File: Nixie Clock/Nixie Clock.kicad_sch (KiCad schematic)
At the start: 101 parts, among them J1 Micro_SD_Card_Det1, Q1 SS8050, Q10 MPSA42/PMBTA42, Q11 MPSA92/PMBTA92, Q12 MPSA42/PMBTA42, Q13 MPSA92/PMBTA92, Q14 MPSA42/PMBTA42, Q15 MPSA92/PMBTA92, Q16 MPSA42/PMBTA42, Q17 MPSA42/PMBTA42, Q18 MPSA42/PMBTA42, Q19 MPSA42/PMBTA42, Q2 SS8050, Q4 MPSA92/PMBTA92, Q5 MPSA42/PMBTA42, Q6 MPSA42/PMBTA42, Q7 MPSA92/PMBTA92, Q8 MPSA42/PMBTA42, Q9 MPSA92/PMBTA92, SW3 SW_MEC_5G, SW4 SW_MEC_5G, U1 ESP32-WROOM-32E, U13 K155NA1, U4 CP2102N-Axx-xQFN28, U6 MCP23017_ML

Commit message: PCB routed
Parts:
- removed N1, N2, N3, N4: IN-6, nixies-us_IN-6, symbol nixies-us:IN-6
- removed NX1, NX2, NX3, NX4, NX5, NX6: IN-12A, nixies-us_IN-12, symbol nixies-us:IN-12A
- removed Q10, Q12, Q14, Q16, Q17, Q18, Q19, Q5, Q6, Q8: MPSA42/PMBTA42, symbol Simulation_SPICE:NPN
- removed Q11, Q13, Q15, Q4, Q7, Q9: MPSA92/PMBTA92, symbol Simulation_SPICE:PNP
- removed R20, R23, R24, R27, R28, R31, R32, R35, R36, R39, R40, R43, R48, R49, R50, R51: 4K7, symbol Device:R
- removed R21, R26, R30, R34, R38, R42: 10K, symbol Device:R
- removed R22, R25, R29, R33, R37, R41: 300K, symbol Device:R
- removed R44, R45, R46, R47: 15K, symbol Device:R
- removed SW3, SW4: SW_MEC_5G, symbol Switch:SW_MEC_5G
- added C11: 10uF, Capacitor_SMD:C_0603_1608Metric, symbol Device:C
- added H1, H2, H3, H4, H5, H6, H7, H8: MountingHole_Pad, MountingHole:MountingHole_3.2mm_M3_Pad_Via, symbol Mechanical:MountingHole_Pad
- added J1: Conn_02x13_Odd_Even, Connector_PinHeader_2.54mm:PinHeader_2x13_P2.54mm_Vertical, symbol Connector_Generic:Conn_02x13_Odd_Even
- added J3: Conn_02x13_Odd_Even, Connector_PinSocket_2.54mm:PinSocket_2x13_P2.54mm_Vertical, symbol Connector_Generic:Conn_02x13_Odd_Even
- added R13, R15, R16, R17: 10K, Resistor_SMD:R_0603_1608Metric, symbol Device:R
- added SW1, SW2: SW_Push, Button_Switch_SMD:SW_Push_SPST_NO_Alps_SKRK, symbol Switch:SW_Push
- C1: renamed from C14; footprint (none) -> Capacitor_SMD:C_0603_1608Metric
- C10: renamed from C2; footprint (none) -> Capacitor_SMD:C_0603_1608Metric
- C2: renamed from C20; footprint (none) -> Capacitor_SMD:C_0603_1608Metric
- C3: renamed from C8; footprint (none) -> Capacitor_SMD:C_0603_1608Metric
- C4: renamed from C9; footprint (none) -> Capacitor_SMD:C_0603_1608Metric
- C5: renamed from C11; footprint (none) -> Capacitor_SMD:C_0603_1608Metric
- C6: renamed from C10; footprint (none) -> Capacitor_SMD:C_0603_1608Metric
- C7: renamed from C12; footprint (none) -> Capacitor_SMD:C_0603_1608Metric
- C8: renamed from C13; footprint (none) -> Capacitor_SMD:C_0603_1608Metric
- C9: renamed from C1; footprint (none) -> Capacitor_SMD:C_0603_1608Metric
- D1: renamed from D11; footprint (none) -> Diode_SMD:D_MiniMELF
- D10: renamed from D19; footprint (none) -> Diode_SMD:D_MiniMELF
- D11: renamed from D20; footprint (none) -> Diode_SMD:D_MiniMELF
- D2: renamed from D12; footprint (none) -> Diode_SMD:D_MiniMELF
- D3: renamed from D13; footprint (none) -> Diode_SMD:D_MiniMELF
- D4: renamed from D14; footprint (none) -> Diode_SMD:D_MiniMELF
- D5: renamed from D15; footprint (none) -> Diode_SMD:D_MiniMELF
- D6: renamed from D21; value ZM4764A 100V -> 1N4764A 100V; footprint (none) -> Diode_THT:D_DO-41_SOD81_P7.62mm_Horizontal
- D7: renamed from D16; footprint (none) -> Diode_SMD:D_MiniMELF
- D8: renamed from D17; footprint (none) -> Diode_SMD:D_MiniMELF
- D9: renamed from D18; footprint (none) -> Diode_SMD:D_MiniMELF
- J2: renamed from J1; footprint (none) -> Connector_Card:microSD_HC_Hirose_DM3AT-SF-PEJM5
- R1: renamed from R16; footprint (none) -> Resistor_SMD:R_0603_1608Metric
- R10: renamed from R14; footprint (none) -> Resistor_SMD:R_0603_1608Metric
- R11: renamed from R15; footprint (none) -> Resistor_SMD:R_0603_1608Metric
- R12: renamed from R1; value 1K -> 10K; footprint (none) -> Resistor_SMD:R_0603_1608Metric
- R14: renamed from R2; footprint (none) -> Resistor_SMD:R_0603_1608Metric
- R2: renamed from R56; footprint (none) -> Resistor_SMD:R_0603_1608Metric
- R3: renamed from R57; footprint (none) -> Resistor_SMD:R_0603_1608Metric
- R4: renamed from R10; footprint (none) -> Resistor_SMD:R_0603_1608Metric
- R5: renamed from R11; footprint (none) -> Resistor_SMD:R_0603_1608Metric
- R6: renamed from R12; footprint (none) -> Resistor_SMD:R_0603_1608Metric
- R7: renamed from R13; footprint (none) -> Resistor_SMD:R_0603_1608Metric
- R8: renamed from R9; footprint (none) -> Resistor_SMD:R_0603_1608Metric
- R9: renamed from R8; footprint (none) -> Resistor_SMD:R_0603_1608Metric
- U1: renamed from U13; footprint (none) -> Package_DIP:DIP-16_W7.62mm
- renumbered U1 to U2, U4 to U3, U6 to U4
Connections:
- net +180V: now also J1.2 (Pin_2), J3.2 (Pin_2)
- net +3.3V: now also C11.1, J1.6 (Pin_6), J3.6 (Pin_6), R13.1, R15.1, R16.1, R17.1
- net +5V: now also J1.3 (Pin_3), J3.3 (Pin_3)
- net EN: now also SW2.2
- net GND: now also C11.2, H1.1, H2.1, H3.1, H4.1, H5.1, H6.1, H7.1, H8.1, J1.1 (Pin_1), J1.4 (Pin_4), J3.1 (Pin_1), J3.4 (Pin_4), SW1.1, SW2.1
- net IO0: now also SW1.2
- net LEDIN: now also J1.5 (Pin_5), J3.5 (Pin_5)
- net MISO: now also R16.2
- net MOSI: now also R15.2
- net N1: now also J1.19 (Pin_19), J3.19 (Pin_19)
- net N2: now also J1.8 (Pin_8), J3.8 (Pin_8)
- net N3: now also J1.14 (Pin_14), J3.14 (Pin_14)
- net N4: now also J1.16 (Pin_16), J3.16 (Pin_16)
- net NCA: now also J1.7 (Pin_7), J3.7 (Pin_7)
- net NCB: now also J1.9 (Pin_9), J3.9 (Pin_9)
- net NCC: now also J1.11 (Pin_11), J3.11 (Pin_11)
- net NCD: now also J1.13 (Pin_13), J3.13 (Pin_13)
- net NX1: now also J1.15 (Pin_15), J3.15 (Pin_15)
- net NX2: now also J1.17 (Pin_17), J3.17 (Pin_17)
- net NX3: now also J1.10 (Pin_10), J3.10 (Pin_10)
- net NX4: now also J1.12 (Pin_12), J3.12 (Pin_12)
- net NX5: now also J1.18 (Pin_18), J3.18 (Pin_18)
- net NX6: now also J1.20 (Pin_20), J3.20 (Pin_20)
- net ROT1A: now also J1.25 (Pin_25), J3.25 (Pin_25)
- net ROT1B: now also J1.23 (Pin_23), J3.23 (Pin_23)
- net ROT1SW: now also J1.21 (Pin_21), J3.21 (Pin_21)
- net ROT2A: now also J1.26 (Pin_26), J3.26 (Pin_26)
- net ROT2B: now also J1.24 (Pin_24), J3.24 (Pin_24)
- net ROT2SW: now also J1.22 (Pin_22), J3.22 (Pin_22)
- net Nixie Tube/0: now reaches D11.2 (A), U1.16 (0)
- net Nixie Tube/1: now reaches D1.2 (A), U1.15 (1)
- net Nixie Tube/2: now reaches D2.2 (A), U1.8 (2)
- net Nixie Tube/3: now reaches D3.2 (A), U1.9 (3)
- net Nixie Tube/4: now reaches D4.2 (A), U1.13 (4)
- net Nixie Tube/5: now reaches D5.2 (A), U1.14 (5)
- net Nixie Tube/6: now reaches D7.2 (A), U1.11 (6)
- net Nixie Tube/7: now reaches D8.2 (A), U1.10 (7)
- net Nixie Tube/8: now reaches D9.2 (A), U1.1 (8)
- net Nixie Tube/9: now reaches D10.2 (A), U1.2 (9)
- net DAT2: now reaches J2.1 (DAT2)
- net DAT2: now also R13.2
- net DAT1: now reaches J2.8 (DAT1)
- net DAT1: now also R17.2
- net CTS: no longer names the net of U3.23 (~{CTS})
- net DCD: no longer names the net of U3.1 (~{DCD})
- net DSR: no longer names the net of U3.27 (~{DSR})
- net RI: no longer names the net of U3.2 (~{RI}/CLK)
- no-connect marks 16 -> 20
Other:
- added sheet Nixie Bulb (nixiebulb.kicad_sch)
- added sheet Nixie Bulb1 (nixiebulb.kicad_sch)
- added sheet Nixie Bulb2 (nixiebulb.kicad_sch)
- added sheet Nixie Bulb3 (nixiebulb.kicad_sch)
- added sheet Nixie Tube (nixietube.kicad_sch)
- added sheet Nixie Tube1 (nixietube.kicad_sch)
- added sheet Nixie Tube2 (nixietube.kicad_sch)
- added sheet Nixie Tube3 (nixietube.kicad_sch)
- added sheet Nixie Tube4 (nixietube.kicad_sch)
- added sheet Nixie Tube5 (nixietube.kicad_sch)
- note added: "B2B Conn"
- note added: "KiCAD Stuff"
- title: (none) -> Nixie Clock
- moved on the sheet: C10, J2, R12, R14

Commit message: Add MAX3421 and CH334R for mass storage device capability
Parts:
- added C54, C55, C59: 100nF, Capacitor_SMD:C_0603_1608Metric, symbol Device:C
- added C56: 10uF, Capacitor_SMD:C_0603_1608Metric, symbol Device:C
- added C57, C58: 18pF, Capacitor_SMD:C_0603_1608Metric, symbol Device:C
- added C60, C61: 1uF, Capacitor_SMD:C_0603_1608Metric, symbol Device:C
- added R75: 10K, Resistor_SMD:R_0603_1608Metric, symbol Device:R
- added R76, R77: 33, Resistor_SMD:R_0603_1608Metric, symbol Device:R
- added U13: CH334R, Package_SO:QSOP-16_3.9x4.9mm_P0.635mm, symbol Interface_USB:CH334R
- added U14: MAX3421EETJ_T, Package_DFN_QFN:HVQFN-32-1EP_5x5mm_P0.5mm_EP3.1x3.1mm, symbol MAX3421EETJ_T:MAX3421EETJ_T
- added Y2, Y3: 12MHz, Crystal:Crystal_SMD_HC49-SD, symbol Device:Crystal
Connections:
- net +3.3V: now also C54.2, C55.2, C56.2, C59.2, C60.2, R75.1, U13.12 (V5), U13.13 (VDD33_{LDO}), U14.2 (VL), U14.23 (VCC)
- net CLK: now also U14.13 (SCLK)
- net Data+: now also U13.11 (DPU+); no longer U3.4 (D+)
- net Data-: now also U13.10 (DMU-); no longer U3.5 (D-)
- net GND: now also C54.1, C55.1, C56.1, C57.2, C58.2, C59.1, C60.1, C61.1, U13.14 (GND), U14.19 (GND), U14.3 (GND), U14.33
- net MISO: now also U14.15 (MISO)
- net MOSI: now also U14.16 (MOSI)
- net ROT2SW: now also U4.3 (GPB6); no longer U2.23 (IO15)
- net VBUS: now also C61.2, U14.22 (VBCOMP)
- new net: U13.15 (XO), Y2.2
- new net: U13.16 (XI), Y2.1
- new net: R77.1, U14.20 (D-)
- new net: R75.2, U14.12 (~{RES})
- new net: R76.2, U14.21 (D+)
- new net: C58.1, U14.24 (XI), Y3.2
- new net: C57.1, U14.25 (XO), Y3.1
- new net CPData+: U13.8 (DP1+), U3.4 (D+)
- new net CPData-: U13.7 (DM1-), U3.5 (D-)
- new net MAXCS: U14.14 (~{SS}), U2.23 (IO15)
- new net MAXData+: R76.1, U13.6 (DP2+)
- new net MAXData-: R77.2, U13.5 (DM2-)
- no-connect marks 20 -> 42
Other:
- moved on the sheet: C1, C10, C11, C2, C3, C4, C5, C6, C7, C8, C9, D1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

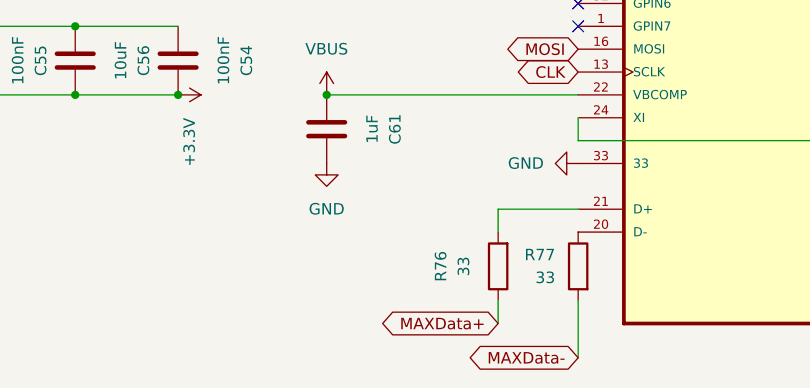
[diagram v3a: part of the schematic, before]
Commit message: Route PCB rev2.1
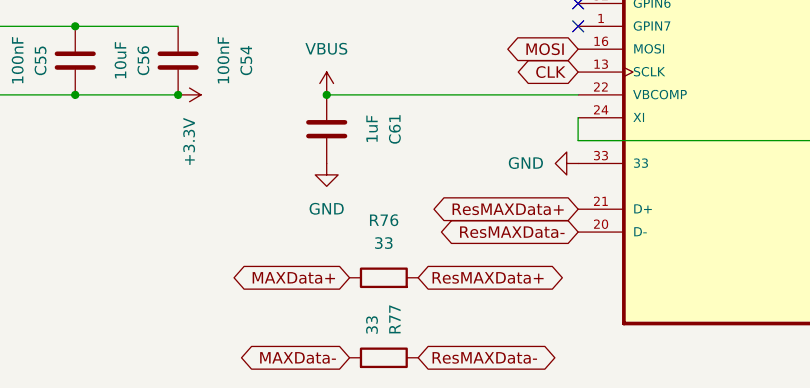
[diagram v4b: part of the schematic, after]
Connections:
- net ResMAXData-: now reaches R77.1, U14.20 (D-)
- net ResMAXData+: now reaches R76.2, U14.21 (D+)
